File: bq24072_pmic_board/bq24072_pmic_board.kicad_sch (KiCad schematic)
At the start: 15 parts, among them J101 USB_B_Micro, J102 Battery, J103 Conn_01x04_Female, U101 AMS1117-3.3

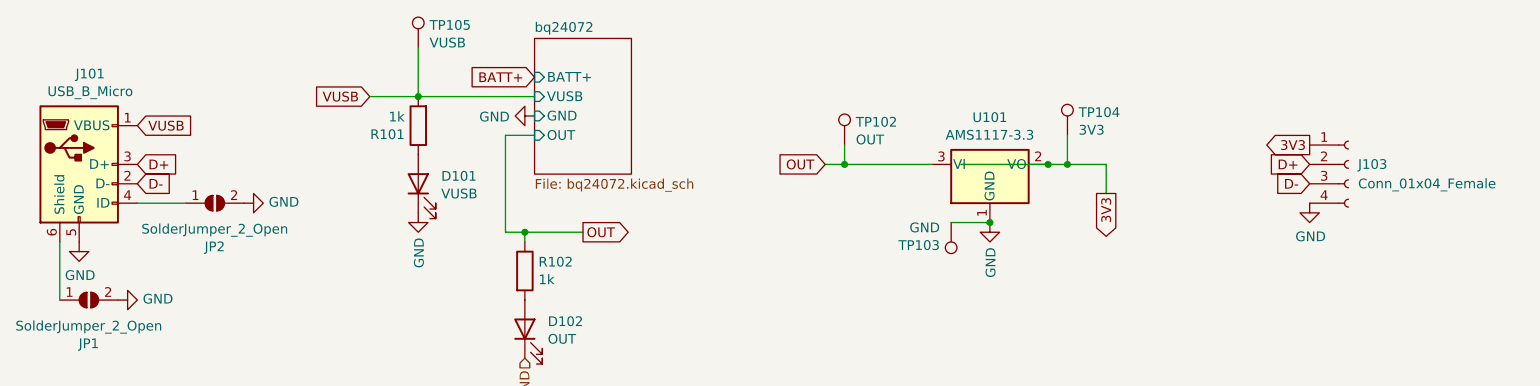
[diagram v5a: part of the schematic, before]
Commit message: [bq24072_pmic_board] Add VBUS output and bump board revision to v2
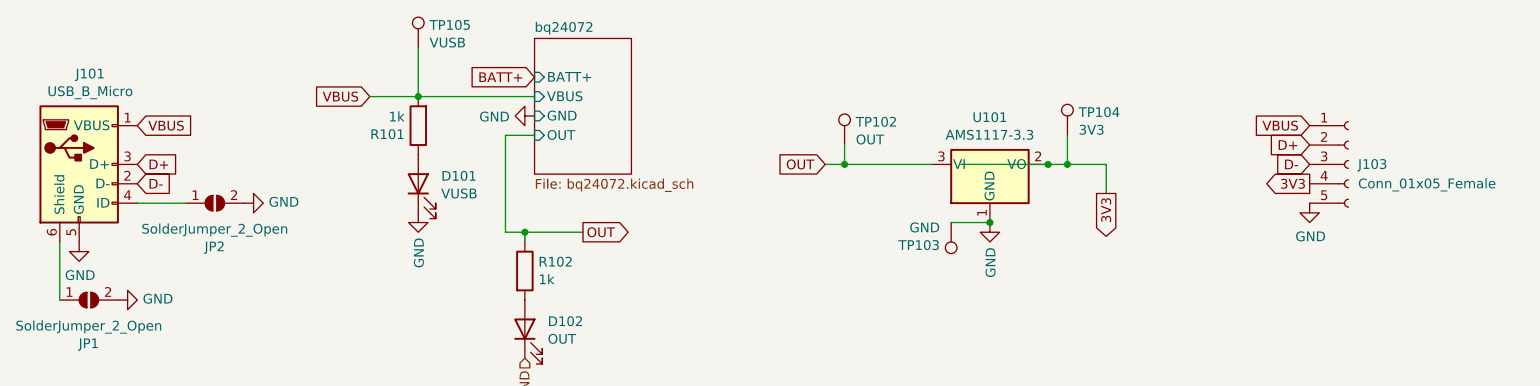
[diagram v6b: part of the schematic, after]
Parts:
- J103: value Conn_01x04_Female -> Conn_01x05_Female; footprint Connector_PinSocket_2.54mm:PinSocket_1x04_P2.54mm_Vertical -> Connector_PinSocket_2.54mm:PinSocket_1x05_P2.54mm_Vertical; symbol Connector:Conn_01x04_Female -> Connector:Conn_01x05_Female
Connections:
- net 3V3: now also J103.4 (Pin_4); no longer J103.1 (Pin_1)
- net GND: now also J103.5 (Pin_5); no longer J103.4 (Pin_4)
- net VUSB renamed VBUS
- net VBUS: now also J103.1 (Pin_1)
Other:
- sheet bq24072 ports: added VBUS; removed VUSB
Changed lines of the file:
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@@
     )
   )
-  (global_label "VUSB" (shape input) (at 100.33 85.09 180) (fields_autoplaced)
-    (effects (font (size 1.27 1.27)) (justify right))
-    (property "Intersheet References" "${INTERSHEET_REFS}" (id 0) (at 146.05 114.3 0)
-      (effects (font (size 1.27 1.27)) hide)
+  (global_label "VBUS" (shape input) (at 100.33 85.09 180) (fields_autoplaced)
+    (effects (font (size 1.27 1.27)) (justify right))
+    (property "Intersheet References" "${INTERSHEET_REFS}" (id 0) (at 93.0183 85.0106 0)
+      (effects (font (size 1.27 1.27)) (justify right) hide)
     )
   )
@@
     )
   )
-  (global_label "D-" (shape input) (at 223.52 96.52 180) (fields_autoplaced)
-    (effects (font (size 1.27 1.27)) (justify right))
-    (property "Intersheet References" "${INTERSHEET_REFS}" (id 0) (at 265.43 133.35 0)
+  (global_label "D-" (shape input) (at 223.52 93.98 180) (fields_autoplaced)
+    (effects (font (size 1.27 1.27)) (justify right))
+    (property "Intersheet References" "${INTERSHEET_REFS}" (id 0) (at 265.43 130.81 0)
       (effects (font (size 1.27 1.27)) hide)
     )
@@
     )
   )
-  (global_label "VUSB" (shape input) (at 69.85 88.9 0) (fields_autoplaced)
+  (global_label "VBUS" (shape input) (at 69.85 88.9 0) (fields_autoplaced)
     (effects (font (size 1.27 1.27)) (justify left))
-    (property "Intersheet References" "${INTERSHEET_REFS}" (id 0) (at 24.13 59.69 0)
-      (effects (font (size 1.27 1.27)) hide)
+    (property "Intersheet References" "${INTERSHEET_REFS}" (id 0) (at 77.1617 88.8206 0)
+      (effects (font (size 1.27 1.27)) (justify left) hide)
     )
   )
@@
     )
   )
-  (global_label "D+" (shape input) (at 223.52 93.98 180) (fields_autoplaced)
-    (effects (font (size 1.27 1.27)) (justify right))
-    (property "Intersheet References" "${INTERSHEET_REFS}" (id 0) (at 265.43 128.27 0)
-      (effects (font (size 1.27 1.27)) hide)
+  (global_label "D+" (shape input) (at 223.52 91.44 180) (fields_autoplaced)
+    (effects (font (size 1.27 1.27)) (justify right))
+    (property "Intersheet References" "${INTERSHEET_REFS}" (id 0) (at 265.43 125.73 0)
+      (effects (font (size 1.27 1.27)) hide)
+    )
+  )
+  (global_label "VBUS" (shape input) (at 223.52 88.9 180) (fields_autoplaced)
+    (effects (font (size 1.27 1.27)) (justify right))
+    (property "Intersheet References" "${INTERSHEET_REFS}" (id 0) (at 216.2083 88.8206 0)
+      (effects (font (size 1.27 1.27)) (justify right) hide)
     )
   )
@@
     )
   )
-  (global_label "3V3" (shape output) (at 223.52 91.44 180) (fields_autoplaced)
-    (effects (font (size 1.27 1.27)) (justify right))
-    (property "Intersheet References" "${INTERSHEET_REFS}" (id 0) (at 314.96 -92.71 0)
+  (global_label "3V3" (shape output) (at 223.52 96.52 180) (fields_autoplaced)
+    (effects (font (size 1.27 1.27)) (justify right))
+    (property "Intersheet References" "${INTERSHEET_REFS}" (id 0) (at 314.96 -87.63 0)
       (effects (font (size 1.27 1.27)) hide)
     )
@@
     (pin "2")
   )
-  (symbol (lib_id "Connector:Conn_01x04_Female") (at 228.6 93.98 0) (unit 1)
+  (symbol (lib_id "Connector:Conn_01x05_Female") (at 228.6 93.98 0) (unit 1)
     (in_bom yes) (on_board yes) (fields_autoplaced)
     (property "Reference" "J103" (id 0) (at 229.87 93.9799 0)
       (effects (font (size 1.27 1.27)) (justify left))
     )
-    (property "Value" "Conn_01x04_Female" (id 1) (at 229.87 96.5199 0)
-      (effects (font (size 1.27 1.27)) (justify left))
-    )
-    (property "Footprint" "Connector_PinSocket_2.54mm:PinSocket_1x04_P2.54mm_Vertical" (id 2) (at 228.6 93.98 0)
+    (property "Value" "Conn_01x05_Female" (id 1) (at 229.87 96.5199 0)
+      (effects (font (size 1.27 1.27)) (justify left))
+    )
+    (property "Footprint" "Connector_PinSocket_2.54mm:PinSocket_1x05_P2.54mm_Vertical" (id 2) (at 228.6 93.98 0)
       (effects (font (size 1.27 1.27)) hide)
     )
@@
     (pin "3")
     (pin "4")
+    (pin "5")
   )
   (symbol (lib_id "Device:R") (at 106.68 88.9 180) (unit 1)
@@
       (effects (font (size 1.27 1.27)) (justify left))
     )
-    (pin "VUSB" input (at 121.92 85.09 180)
-      (effects (font (size 1.27 1.27)) (justify left))
-    )
     (pin "OUT" input (at 121.92 90.17 180)
+      (effects (font (size 1.27 1.27)) (justify left))
+    )
+    (pin "VBUS" input (at 121.92 85.09 180)
       (effects (font (size 1.27 1.27)) (justify left))
     )
@@
     )
     (path "/e6370a18-df10-4e5b-9423-b0399ccd17a5"
-      (reference "J103") (unit 1) (value "Conn_01x04_Female") (footprint "Connector_PinSocket_2.54mm:PinSocket_1x04_P2.54mm_Vertical")
+      (reference "J103") (unit 1) (value "Conn_01x05_Female") (footprint "Connector_PinSocket_2.54mm:PinSocket_1x05_P2.54mm_Vertical")
     )
     (path "/9b315454-a4a0-4952-bdbe-d4a8e96c16f9"
